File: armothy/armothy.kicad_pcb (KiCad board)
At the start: 2 copper layers, 21 parts, among them J1 I2C, J2 UART, J3 motZ, J4 pump, J5 valve, J6 Encoder, J7 Limit switch, J8 12V_PWR, J9 Conn_01x03_Female, U1 L293D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

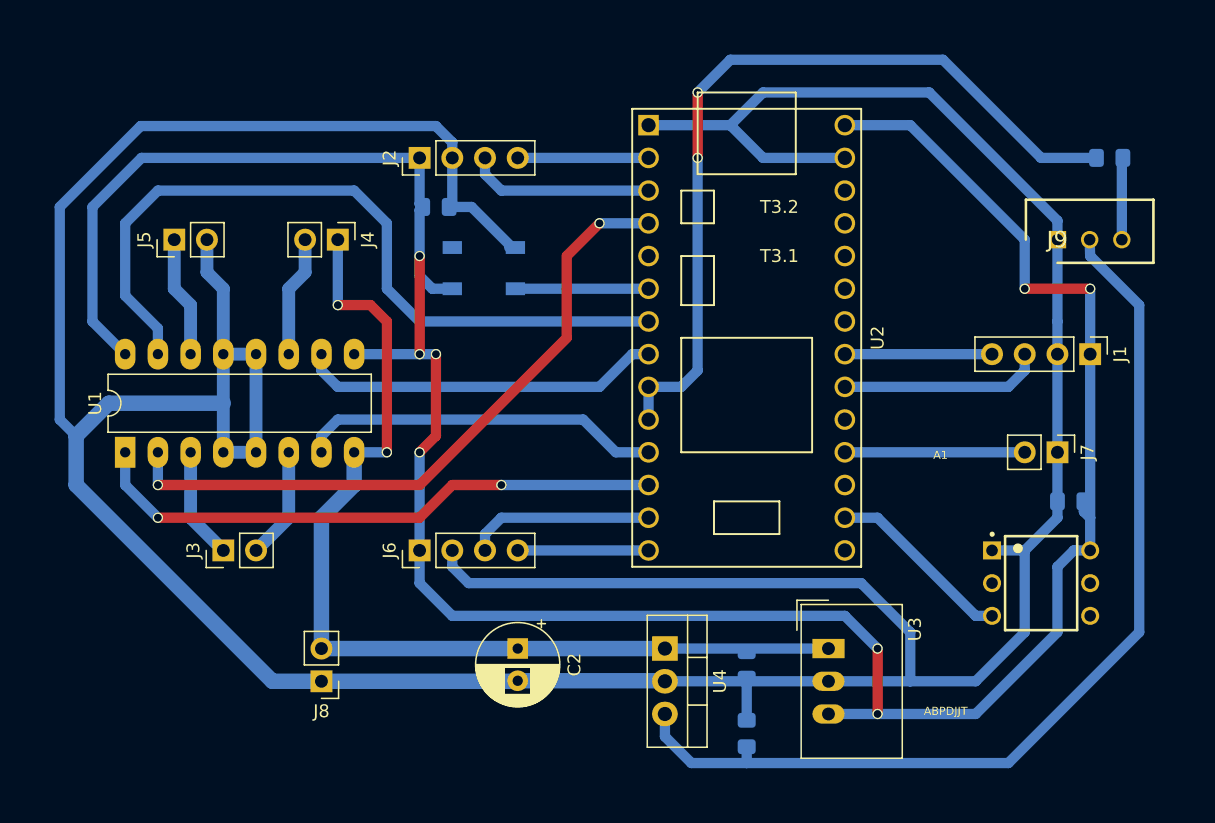
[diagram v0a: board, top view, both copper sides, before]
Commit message: Improve libraries management; Adds Dynamixel connector 3D model (fix #4).
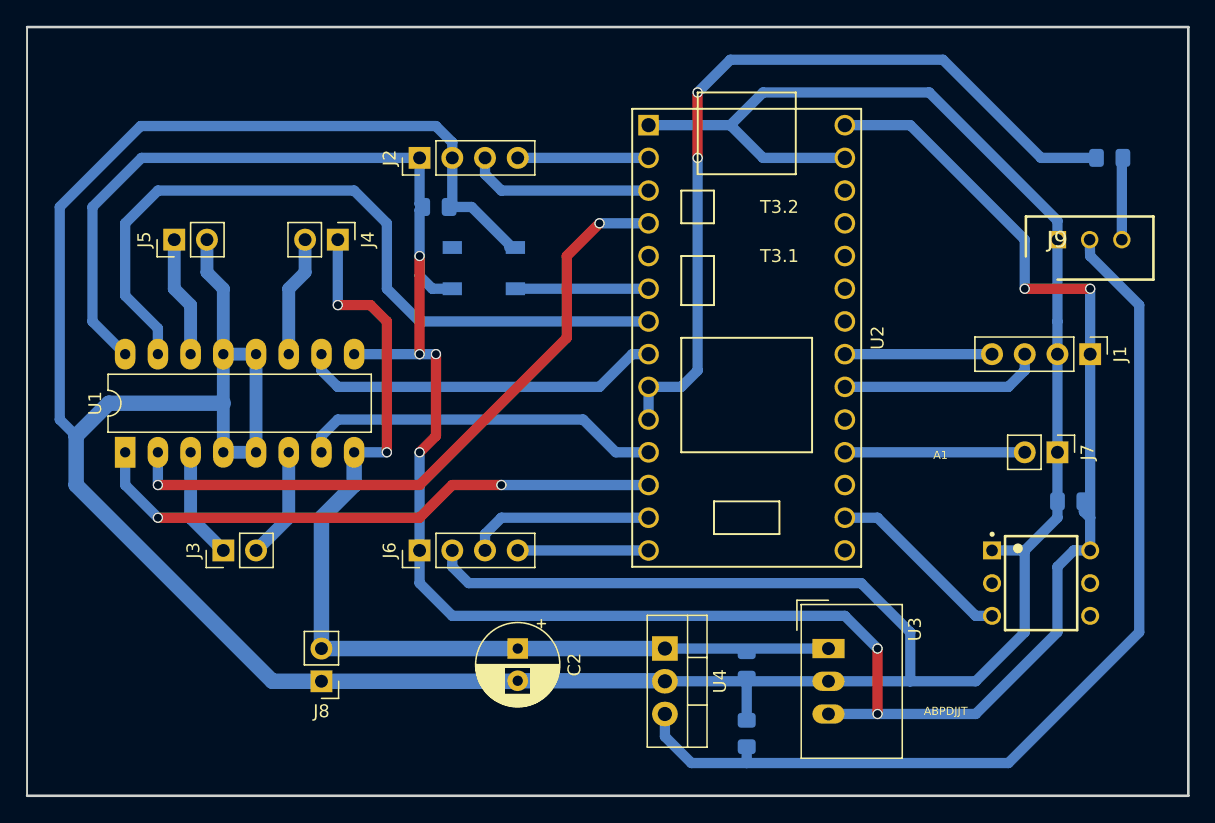
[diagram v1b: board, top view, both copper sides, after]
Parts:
- J9: footprint 22-03-5035:SHDR3W70P0X250_1X3_990X490X590P -> molex_22035XXX:SHDR3W70P0X250_1X3_990X490X590P
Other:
- board outline added: 90.2 x 59.7 mm
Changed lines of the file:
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@@
   (general
     (thickness 1.6)
-    (drawings 0)
+    (drawings 4)
     (tracks 198)
     (zones 0)
@@
   )
   (setup
-    (last_trace_width 0.8)
+    (last_trace_width 0.508)
     (user_trace_width 0.3)
     (user_trace_width 0.5)
@@
     (add_net "Net-(U2-Pad31)")
     (add_net "Net-(U2-Pad5)")
+  )
+  (module molex_22035XXX:SHDR3W70P0X250_1X3_990X490X590P (layer F.Cu)
+    (at 158.75 74.93 180)
+    (descr 22-03-5035)
+    (tags Connector)
+    (fp_text reference J9 (at 0 0 180) (layer F.SilkS)
+      (effects (font (size 1.27 1.27) (thickness 0.254)))
+    )
+    (fp_text value Conn_01x03_Female (at 0 0 180) (layer F.SilkS) hide
+      (effects (font (size 1.27 1.27) (thickness 0.254)))
+    )
+    (fp_line (start 2.45 1.8) (end 2.45 -1.3) (layer F.SilkS) (width 0.2))
+    (fp_line (start -7.45 1.8) (end 2.45 1.8) (layer F.SilkS) (width 0.2))
+    (fp_line (start -7.45 -3.1) (end -7.45 1.8) (layer F.SilkS) (width 0.2))
+    (fp_line (start 0 -3.1) (end -7.45 -3.1) (layer F.SilkS) (width 0.2))
+    (fp_line (start 2.45 1.8) (end 2.45 -3.1) (layer Dwgs.User) (width 0.1))
+    (fp_line (start -7.45 1.8) (end 2.45 1.8) (layer Dwgs.User) (width 0.1))
+    (fp_line (start -7.45 -3.1) (end -7.45 1.8) (layer Dwgs.User) (width 0.1))
+    (fp_line (start 2.45 -3.1) (end -7.45 -3.1) (layer Dwgs.User) (width 0.1))
+    (fp_line (start 2.7 2) (end 2.7 -3.4) (layer Dwgs.User) (width 0.05))
+    (fp_line (start -7.7 2) (end 2.7 2) (layer Dwgs.User) (width 0.05))
+    (fp_line (start -7.7 -3.4) (end -7.7 2) (layer Dwgs.User) (width 0.05))
+    (fp_line (start 2.7 -3.4) (end -7.7 -3.4) (layer Dwgs.User) (width 0.05))
+    (pad 3 thru_hole circle (at -5 0 270) (size 1.35 1.35) (drill 0.9) (layers *.Cu *.Mask F.SilkS)
+      (net 25 "Net-(J9-Pad3)"))
+    (pad 2 thru_hole circle (at -2.5 0 270) (size 1.35 1.35) (drill 0.9) (layers *.Cu *.Mask F.SilkS)
+      (net 19 +10V))
+    (pad 1 thru_hole rect (at 0 0 270) (size 1.35 1.35) (drill 0.9) (layers *.Cu *.Mask F.SilkS)
+      (net 1 GND))
+    (model ${CUSTOM_3D}/molex_22035XXX.3dshapes/022035035.stp.wrl
+      (at (xyz 0 0 0))
+      (scale (xyz 1 1 1))
+      (rotate (xyz 0 0 0))
+    )
   )
   (module Capacitor_SMD:C_0805_2012Metric_Pad1.15x1.40mm_HandSolder (layer B.Cu)
@@
     )
   )
-  (module 22-03-5035:SHDR3W70P0X250_1X3_990X490X590P (layer F.Cu)
-    (at 158.75 74.93 180)
-    (descr 22-03-5035)
-    (tags Connector)
-    (fp_text reference J9 (at 0 0 180) (layer F.SilkS)
-      (effects (font (size 1.27 1.27) (thickness 0.254)))
-    )
-    (fp_text value Conn_01x03_Female (at 0 0 180) (layer F.SilkS) hide
-      (effects (font (size 1.27 1.27) (thickness 0.254)))
-    )
-    (fp_line (start 2.7 -2.05) (end -7.7 -2.05) (layer Dwgs.User) (width 0.05))
-    (fp_line (start -7.7 -2.05) (end -7.7 3.35) (layer Dwgs.User) (width 0.05))
-    (fp_line (start -7.7 3.35) (end 2.7 3.35) (layer Dwgs.User) (width 0.05))
-    (fp_line (start 2.7 3.35) (end 2.7 -2.05) (layer Dwgs.User) (width 0.05))
-    (fp_line (start 2.45 -1.8) (end -7.45 -1.8) (layer Dwgs.User) (width 0.1))
-    (fp_line (start -7.45 -1.8) (end -7.45 3.1) (layer Dwgs.User) (width 0.1))
-    (fp_line (start -7.45 3.1) (end 2.45 3.1) (layer Dwgs.User) (width 0.1))
-    (fp_line (start 2.45 3.1) (end 2.45 -1.8) (layer Dwgs.User) (width 0.1))
-    (fp_line (start 0 -1.8) (end -7.45 -1.8) (layer F.SilkS) (width 0.2))
-    (fp_line (start -7.45 -1.8) (end -7.45 3.1) (layer F.SilkS) (width 0.2))
-    (fp_line (start -7.45 3.1) (end 2.45 3.1) (layer F.SilkS) (width 0.2))
-    (fp_line (start 2.45 3.1) (end 2.45 0) (layer F.SilkS) (width 0.2))
-    (pad 1 thru_hole rect (at 0 0 270) (size 1.35 1.35) (drill 0.9) (layers *.Cu *.Mask F.SilkS)
-      (net 1 GND))
-    (pad 2 thru_hole circle (at -2.5 0 270) (size 1.35 1.35) (drill 0.9) (layers *.Cu *.Mask F.SilkS)
-      (net 19 +10V))
-    (pad 3 thru_hole circle (at -5 0 270) (size 1.35 1.35) (drill 0.9) (layers *.Cu *.Mask F.SilkS)
-      (net 25 "Net-(J9-Pad3)"))
-  )
   (module Package_DIP:DIP-16_W7.62mm_LongPads (layer F.Cu)
     (at 86.36 91.44 90)
@@
     )
   )
+  (gr_line (start 78.74 118.11) (end 78.74 58.42) (layer Edge.Cuts) (width 0.15))
+  (gr_line (start 168.91 118.11) (end 78.74 118.11) (layer Edge.Cuts) (width 0.2))
+  (gr_line (start 168.91 58.42) (end 168.91 118.11) (layer Edge.Cuts) (width 0.2))
+  (gr_line (start 78.74 58.42) (end 168.91 58.42) (layer Edge.Cuts) (width 0.2))
   (segment (start 158.75 91.44) (end 158.75 83.82) (width 0.8) (layer B.Cu) (net 1))
   (segment (start 92.71 74.93) (end 92.71 77.47) (width 1) (layer B.Cu) (net 1))
